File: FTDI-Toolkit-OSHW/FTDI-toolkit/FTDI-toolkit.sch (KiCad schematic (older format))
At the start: 81 parts, among them IC1 TLV70033DCKT, IC12 SN74LV1T125DCKR, IC13 74HC00BQ, IC15 TS5A3359, IC2 TLV70018DCKT, IC3 TS5A3359, IC7 SN74LV1T125DCKR, IC8 FT2232D, Y1 MQ-6.000-12-30/30/

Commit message: Schematic review
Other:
- note added: "Review connections!!!!"
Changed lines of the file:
@@
 Wire Wire Line
 	6450 5800 6600 5800
+Text Notes 13750 1750 0    118  ~ 24
+Review connections!!!!
 $EndSCHEMATC

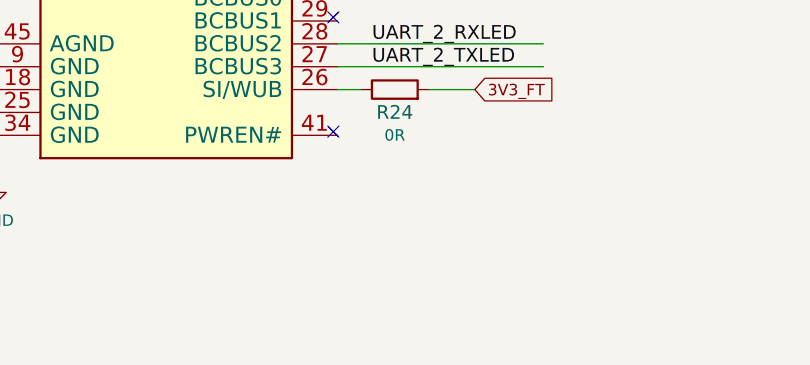
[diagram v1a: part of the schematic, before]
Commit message: Add logotypes to PCB
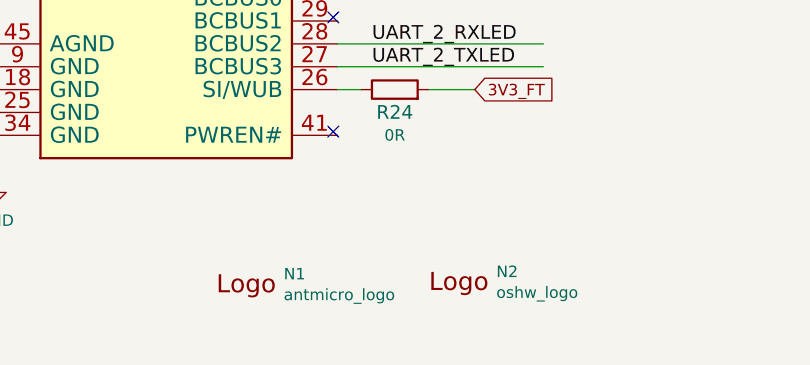
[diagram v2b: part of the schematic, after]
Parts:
- added N1: antmicro_logo, FTDI-toolkit:antmicro-logo_scaled_12mm, symbol FTDI-toolkit:antmicro_logo
- added N2: oshw_logo, FTDI-toolkit:OSHW-Logo2_7.3x6mm_SilkScreen, symbol FTDI-toolkit:oshw_logo
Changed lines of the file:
@@
 Text Notes 13750 1750 0    118  ~ 24
 Review connections!!!!
+$Comp
+L FTDI-toolkit:antmicro_logo N1
+U 1 1 5E6C149E
+P 10100 10950
+F 0 "N1" H 10314 11043 50  0000 L CNN
+F 1 "antmicro_logo" H 10314 10952 50  0000 L CNN
+F 2 "FTDI-toolkit:antmicro-logo_scaled_12mm" H 10000 11200 50  0001 C CNN
+F 3 "" H 10100 11300 50  0001 C CNN
+	1    10100 10950
+	1    0    0    -1
+$EndComp
+$Comp
+L FTDI-toolkit:oshw_logo N2
+U 1 1 5E6EE219
+P 11050 10850
+F 0 "N2" H 11244 10853 50  0000 L CNN
+F 1 "oshw_logo" H 11244 10762 50  0000 L CNN
+F 2 "FTDI-toolkit:OSHW-Logo2_7.3x6mm_SilkScreen" H 11070 10610 50  0001 C CNN
+F 3 "" H 11050 10850 50  0001 C CNN
+	1    11050 10850
+	1    0    0    -1
+$EndComp
 $EndSCHEMATC
